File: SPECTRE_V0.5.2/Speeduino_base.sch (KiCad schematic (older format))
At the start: 218 parts, among them J1 Conn_01x06_Male, J2 Conn_02x04_Odd_Even, J3 ProtoArea, Q1 AO3400, Q10 BSP78, Q11 BSP78, Q12 AO3400, Q13 BSP78, Q14 BSP78, Q15 BSP78, Q16 BSP78, Q17 BSP78, Q18 BSP78, Q19 BSP78, Q20 BSP78, Q21 BSP78, Q6 AO3400, Q7 AO3400, Q8 AO3400, Q9 AO3400, U1 MAX9926UAEE+, U2 LM78M05_TO220, U3 TL431DBZ, U4 molex_48pin, U5 TJA1050, U6 MAX3232, U7 MIC4427, U8 MIC4427, U9 MIC4427

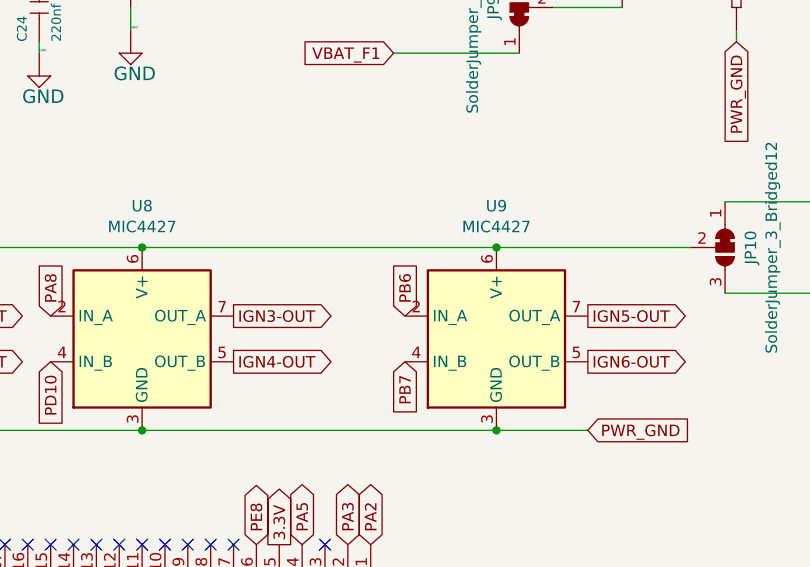
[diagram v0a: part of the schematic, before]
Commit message: Update ign5 pin
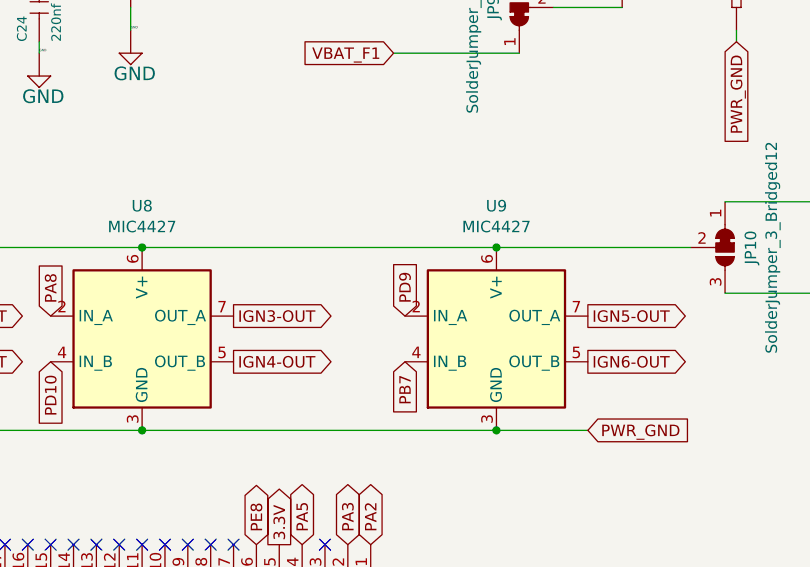
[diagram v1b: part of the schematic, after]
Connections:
- net PB6: no longer U9.2 (IN_A)
- net PD9: now also U9.2 (IN_A)
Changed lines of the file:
@@
 $EndComp
 Text GLabel 8300 9550 1    50   Input ~ 0
-PB6
+PD9
 Text GLabel 9100 10050 2    50   Input ~ 0
 PWR_GND

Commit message: Updates on V0.5.2
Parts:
- removed D24, D25: 1N4007, Diode_SMD:D_SMA, symbol Device:D_Small
- removed JP17: SolderJumper_3_Bridged12, Jumper:SolderJumper-3_P1.3mm_Bridged12_Pad1.0x1.5mm, symbol Jumper:SolderJumper_3_Bridged12
- removed Q8, Q9: AO3400, Speeduino_base:SOT-23, symbol Speeduino_base-eagle-import:SMD-MOSFET-N-CH-20V-2.1A-CJ2302(SOT-23)
- removed R70, R71: 100R, Speeduino_base:R0603, symbol Speeduino_base-eagle-import:SMD-RES-470R-5%-1_10W(0603)
- removed R72, R73: 10k, Speeduino_base:R0603, symbol Speeduino_base-eagle-import:SMD-RES-470R-5%-1_10W(0603)
- added JP18: SolderJumper_3_Bridged12, Jumper:SolderJumper-3_P1.3mm_Bridged12_Pad1.0x1.5mm, symbol Jumper:SolderJumper_3_Bridged12
- added U10: MIC4427, Package_SO:SO-8_3.9x4.9mm_P1.27mm, symbol Driver_FET:MIC4427
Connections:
- net FLEX_FUEL_IN: now also U4.38; no longer JP16.1 (A)
- net GND: now also JP16.1 (A), JP18.1 (A); no longer U4.22, U4.26
- net IGN5-OUT: now also JP18.3 (B); no longer JP16.3 (B)
- net IGN6-OUT: now also JP16.3 (B)
- net PB12: now also U10.2 (IN_A)
- net PB13: now also U10.4 (IN_B)
- net PWR_GND: now also U10.3 (GND)
- net Spare_1-Out: now also U10.5 (OUT_B)
- net Spare_2-Out: now also U10.7 (OUT_A)
- net TACHO-OUT: now also U4.48
- net V_IDLE: now also U10.6 (V+)
- net at JP16.2 (C): now also U4.26; no longer U4.38
- new net: JP18.2 (C), U4.22
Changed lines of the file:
@@
 Text GLabel 6500 1400 3    50   Output ~ 0
 MAP
-Text GLabel 6600 1400 3    50   Input ~ 0
-GND
 Text GLabel 5650 1400 3    50   Output ~ 0
 IAT
@@
 Text GLabel 8850 1400 3    50   Input ~ 0
 3.3V
-Text GLabel 8200 2050 3    50   Output ~ 0
+Text GLabel 7950 1400 3    50   Output ~ 0
 FLEX_FUEL_IN
-Text GLabel 9350 2000 3    50   Input ~ 0
-TACHO-OUT
 $Comp
 L Jumper:SolderJumper_3_Bridged12 JP8
@@
 Wire Wire Line
 	750  10300 750  10400
-Text GLabel 6200 1400 3    50   Input ~ 0
+Text GLabel 7450 2300 3    50   Input ~ 0
 GND
 Text GLabel 7050 1400 3    50   Input ~ 0
@@
 Wire Wire Line
 	4050 11100 4050 11200
-Text GLabel 11850 9400 2    50   Input ~ 0
+Text GLabel 11800 9500 2    50   Input ~ 0
 PWR_GND
-Text GLabel 12300 8850 1    50   Output ~ 0
+Text GLabel 12150 8950 2    50   Output ~ 0
 Spare_2-Out
-Text GLabel 11950 8550 0    50   Input ~ 0
-VBAT
-Wire Wire Line
-	11400 9400 11800 9400
-Wire Wire Line
-	11400 9050 11600 9050
-Wire Wire Line
-	11250 9000 11400 9000
-Wire Wire Line
-	11400 9000 11400 9050
-Connection ~ 11400 9050
-Wire Wire Line
-	11400 9350 11400 9400
-Wire Wire Line
-	11800 9400 11800 9250
-Wire Wire Line
-	11800 8850 11950 8850
-$Comp
-L Speeduino_base-eagle-import:SMD-RES-470R-5%-1_10W(0603) R73
-U 1 1 5F3D9256
-P 11400 9200
-F 0 "R73" H 11250 9250 42  0000 L BNN
-F 1 "10k" H 11250 9100 42  0000 L BNN
-F 2 "Speeduino_base:R0603" H 11400 9200 50  0001 C CNN
-F 3 "" H 11400 9200 50  0001 C CNN
-	1    11400 9200
-	0    1    1    0
-$EndComp
-$Comp
-L Speeduino_base-eagle-import:SMD-RES-470R-5%-1_10W(0603) R71
-U 1 1 5F3D9262
-P 11100 9000
-F 0 "R71" H 10950 9050 42  0000 L BNN
-F 1 "100R" H 10950 8900 42  0000 L BNN
-F 2 "Speeduino_base:R0603" H 11100 9000 50  0001 C CNN
-F 3 "" H 11100 9000 50  0001 C CNN
-	1    11100 9000
-	1    0    0    -1
-$EndComp
-$Comp
-L Speeduino_base-eagle-import:SMD-MOSFET-N-CH-20V-2.1A-CJ2302(SOT-23) Q9
-U 1 1 5F3D9268
-P 11800 9050
-F 0 "Q9" H 11650 9150 42  0000 L BNN
-F 1 "AO3400" H 11800 9150 42  0000 L BNN
-F 2 "Speeduino_base:SOT-23" H 11800 9050 50  0001 C CNN
-F 3 "" H 11800 9050 50  0001 C CNN
-	1    11800 9050
-	1    0    0    -1
-$EndComp
-$Comp
-L Device:D_Small D25
-U 1 1 5F3D926E
-P 11950 8750
-F 0 "D25" V 11904 8818 50  0000 L CNN
-F 1 "1N4007" V 11995 8818 50  0000 L CNN
-F 2 "Diode_SMD:D_SMA" V 11950 8750 50  0001 C CNN
-F 3 "~" V 11950 8750 50  0001 C CNN
-	1    11950 8750
-	0    1    1    0
-$EndComp
-Wire Wire Line
-	11950 8850 12300 8850
-Connection ~ 11950 8850
-Text GLabel 10850 9000 1    50   Input ~ 0
+Text GLabel 11750 8650 0    50   Input ~ 0
+V_IDLE
+Text GLabel 11300 9150 0    50   Input ~ 0
 PB13
-Wire Wire Line
-	10850 9000 10950 9000
-Wire Wire Line
-	11850 9400 11800 9400
-Connection ~ 11800 9400
-Wire Wire Line
-	11950 8550 11950 8650
-Text GLabel 11850 8150 2    50   Input ~ 0
-PWR_GND
-Text GLabel 12300 7600 1    50   Output ~ 0
+Text GLabel 12200 9150 2    50   Output ~ 0
 Spare_1-Out
-Text GLabel 11950 7300 0    50   Input ~ 0
-VBAT
-Wire Wire Line
-	11400 8150 11800 8150
-Wire Wire Line
-	11400 7800 11600 7800
-Wire Wire Line
-	11250 7750 11400 7750
-Wire Wire Line
-	11400 7750 11400 7800
-Connection ~ 11400 7800
-Wire Wire Line
-	11400 8100 11400 8150
-Wire Wire Line
-	11800 8150 11800 8000
-Wire Wire Line
-	11800 7600 11950 7600
-$Comp
-L Speeduino_base-eagle-import:SMD-RES-470R-5%-1_10W(0603) R72
-U 1 1 5F7FAD08
-P 11400 7950
-F 0 "R72" H 11250 8000 42  0000 L BNN
-F 1 "10k" H 11250 7850 42  0000 L BNN
-F 2 "Speeduino_base:R0603" H 11400 7950 50  0001 C CNN
-F 3 "" H 11400 7950 50  0001 C CNN
-	1    11400 7950
-	0    1    1    0
-$EndComp
-$Comp
-L Speeduino_base-eagle-import:SMD-RES-470R-5%-1_10W(0603) R70
-U 1 1 5F7FAD0E
-P 11100 7750
-F 0 "R70" H 10950 7800 42  0000 L BNN
-F 1 "100R" H 10950 7650 42  0000 L BNN
-F 2 "Speeduino_base:R0603" H 11100 7750 50  0001 C CNN
-F 3 "" H 11100 7750 50  0001 C CNN
-	1    11100 7750
-	1    0    0    -1
-$EndComp
-$Comp
-L Speeduino_base-eagle-import:SMD-MOSFET-N-CH-20V-2.1A-CJ2302(SOT-23) Q8
-U 1 1 5F7FAD14
-P 11800 7800
-F 0 "Q8" H 11650 7900 42  0000 L BNN
-F 1 "AO3400" H 11800 7900 42  0000 L BNN
-F 2 "Speeduino_base:SOT-23" H 11800 7800 50  0001 C CNN
-F 3 "" H 11800 7800 50  0001 C CNN
-	1    11800 7800
-	1    0    0    -1
-$EndComp
-$Comp
-L Device:D_Small D24
-U 1 1 5F7FAD1A
-P 11950 7500
-F 0 "D24" V 11904 7568 50  0000 L CNN
-F 1 "1N4007" V 11995 7568 50  0000 L CNN
-F 2 "Diode_SMD:D_SMA" V 11950 7500 50  0001 C CNN
-F 3 "~" V 11950 7500 50  0001 C CNN
-	1    11950 7500
-	0    1    1    0
-$EndComp
-Wire Wire Line
-	11950 7600 12300 7600
-Connection ~ 11950 7600
-Text GLabel 10850 7750 1    50   Input ~ 0
+Text GLabel 11350 8950 0    50   Input ~ 0
 PB12
-Wire Wire Line
-	10850 7750 10950 7750
-Wire Wire Line
-	11850 8150 11800 8150
-Connection ~ 11800 8150
-Wire Wire Line
-	11950 7300 11950 7400
 Text GLabel 16450 10950 2    50   Output ~ 0
 INJ8-OUT
@@
 Connection ~ 7150 10050
 Connection ~ 8700 10050
-$Comp
-L Jumper:SolderJumper_3_Bridged12 JP16
-U 1 1 5F69F1FE
-P 7950 2000
-F 0 "JP16" H 7950 2113 50  0000 C CNN
-F 1 "SolderJumper_3_Bridged12" H 7950 2204 50  0000 C CNN
-F 2 "Jumper:SolderJumper-3_P1.3mm_Bridged12_Pad1.0x1.5mm" H 7950 2000 50  0001 C CNN
-F 3 "~" H 7950 2000 50  0001 C CNN
-	1    7950 2000
-	-1   0    0    1
-$EndComp
-Text GLabel 7750 2100 3    50   Input ~ 0
-IGN5-OUT
-Wire Wire Line
-	7750 2000 7750 2100
-Wire Wire Line
-	8150 2000 8200 2000
-Wire Wire Line
-	8200 2000 8200 2050
-Wire Wire Line
-	7950 1400 7950 1850
-$Comp
-L Jumper:SolderJumper_3_Bridged12 JP17
-U 1 1 5F83750C
-P 9150 2000
-F 0 "JP17" H 9150 2113 50  0000 C CNN
-F 1 "SolderJumper_3_Bridged12" H 9150 2204 50  0000 C CNN
-F 2 "Jumper:SolderJumper-3_P1.3mm_Bridged12_Pad1.0x1.5mm" H 9150 2000 50  0001 C CNN
-F 3 "~" H 9150 2000 50  0001 C CNN
-	1    9150 2000
-	-1   0    0    1
-$EndComp
-Text GLabel 8950 2100 3    50   Input ~ 0
-IGN6-OUT
-Wire Wire Line
-	8950 2000 8950 2100
-Wire Wire Line
-	9150 1850 9150 1400
-Wire Wire Line
-	9150 1400 9050 1400
 Text GLabel 7450 11050 3    50   Input ~ 0
 5V
@@
 Text GLabel 2600 2350 3    50   Input ~ 0
 5V
+$Comp
+L Jumper:SolderJumper_3_Bridged12 JP18
+U 1 1 5F36B798
+P 7200 2250
+F 0 "JP18" H 7200 2363 50  0000 C CNN
+F 1 "SolderJumper_3_Bridged12" H 7200 2454 50  0000 C CNN
+F 2 "Jumper:SolderJumper-3_P1.3mm_Bridged12_Pad1.0x1.5mm" H 7200 2250 50  0001 C CNN
+F 3 "~" H 7200 2250 50  0001 C CNN
+	1    7200 2250
+	-1   0    0    1
+$EndComp
+Text GLabel 7000 2350 3    50   Input ~ 0
+IGN5-OUT
+Wire Wire Line
+	7000 2250 7000 2350
+Wire Wire Line
+	7400 2250 7450 2250
+Wire Wire Line
+	7450 2250 7450 2300
+Wire Wire Line
+	7200 2100 6650 2100
+Wire Wire Line
+	6650 2100 6650 1900
+Wire Wire Line
+	6650 1900 6200 1900
+Wire Wire Line
+	6200 1900 6200 1400
+Text GLabel 9050 1400 3    50   Input ~ 0
+TACHO-OUT
+Text GLabel 8100 2300 3    50   Input ~ 0
+GND
+$Comp
+L Jumper:SolderJumper_3_Bridged12 JP16
+U 1 1 5F462689
+P 7850 2250
+F 0 "JP16" H 7850 2363 50  0000 C CNN
+F 1 "SolderJumper_3_Bridged12" H 7850 2454 50  0000 C CNN
+F 2 "Jumper:SolderJumper-3_P1.3mm_Bridged12_Pad1.0x1.5mm" H 7850 2250 50  0001 C CNN
+F 3 "~" H 7850 2250 50  0001 C CNN
+	1    7850 2250
+	-1   0    0    1
+$EndComp
+Text GLabel 7650 2350 3    50   Input ~ 0
+IGN6-OUT
+Wire Wire Line
+	7650 2250 7650 2350
+Wire Wire Line
+	8050 2250 8100 2250
+Wire Wire Line
+	8100 2250 8100 2300
+Wire Wire Line
+	7850 2100 7850 2000
+Wire Wire Line
+	7850 2000 6700 2000
+Wire Wire Line
+	6700 2000 6700 1700
+Wire Wire Line
+	6700 1700 6600 1700
+Wire Wire Line
+	6600 1700 6600 1400
+$Comp
+L Driver_FET:MIC4427 U10
+U 1 1 5F558FC7
+P 11750 9050
+F 0 "U10" H 11750 9631 50  0000 C CNN
+F 1 "MIC4427" H 11750 9540 50  0000 C CNN
+F 2 "Package_SO:SO-8_3.9x4.9mm_P1.27mm" H 11750 8750 50  0001 C CNN
+F 3 "http://ww1.microchip.com/downloads/en/DeviceDoc/mic4426.pdf" H 11750 8750 50  0001 C CNN
+	1    11750 9050
+	1    0    0    -1
+$EndComp
+Wire Wire Line
+	11750 9450 11750 9500
+Wire Wire Line
+	11750 9500 11800 9500
+Wire Wire Line
+	11350 9150 11300 9150
+Wire Wire Line
+	12150 9150 12200 9150
 $EndSCHEMATC

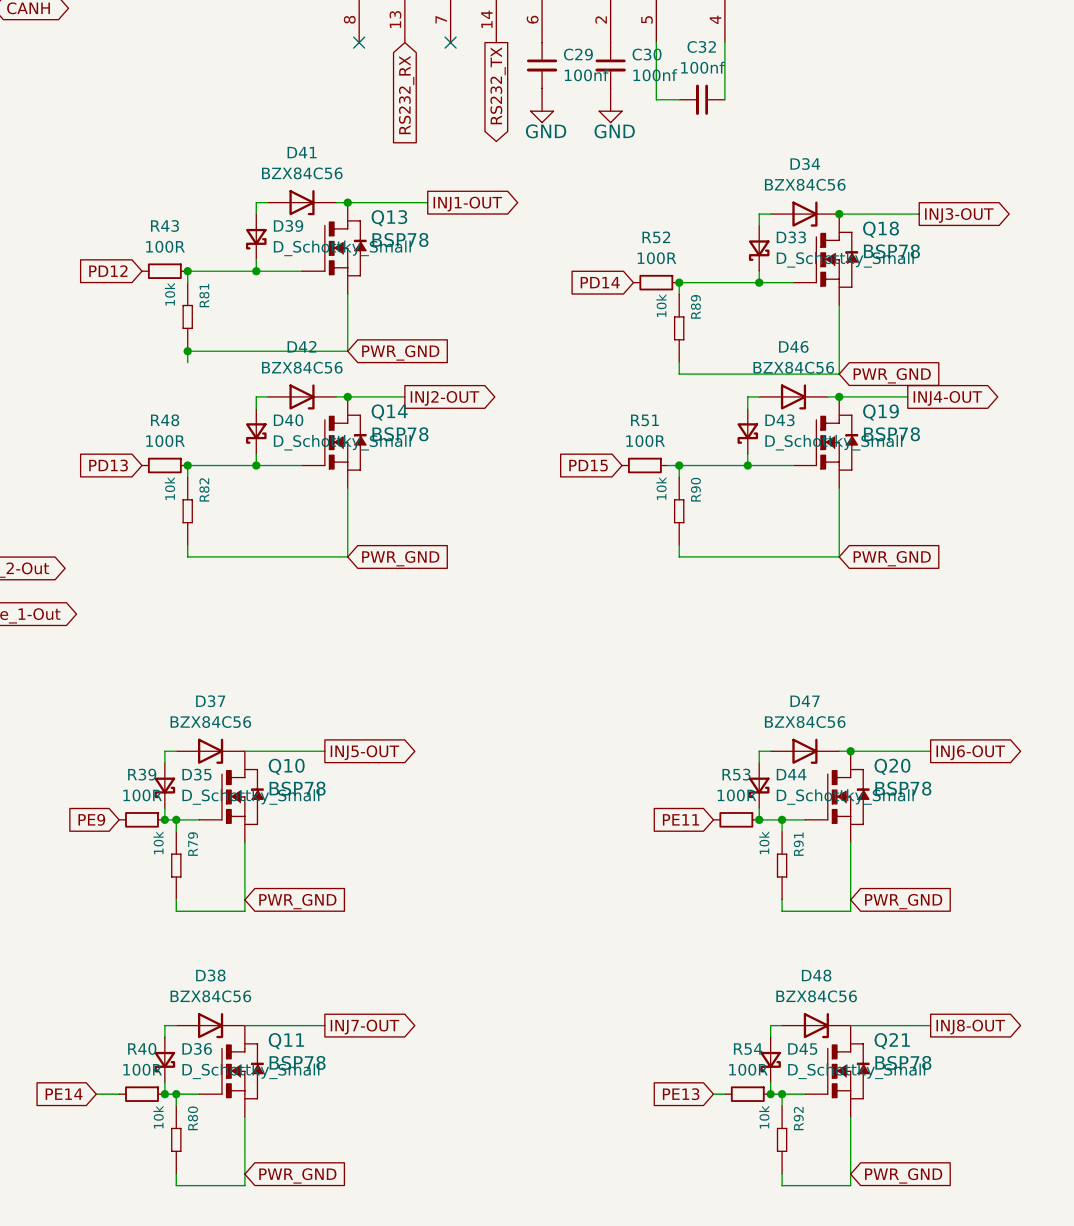
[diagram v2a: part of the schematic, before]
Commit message: Update zener value
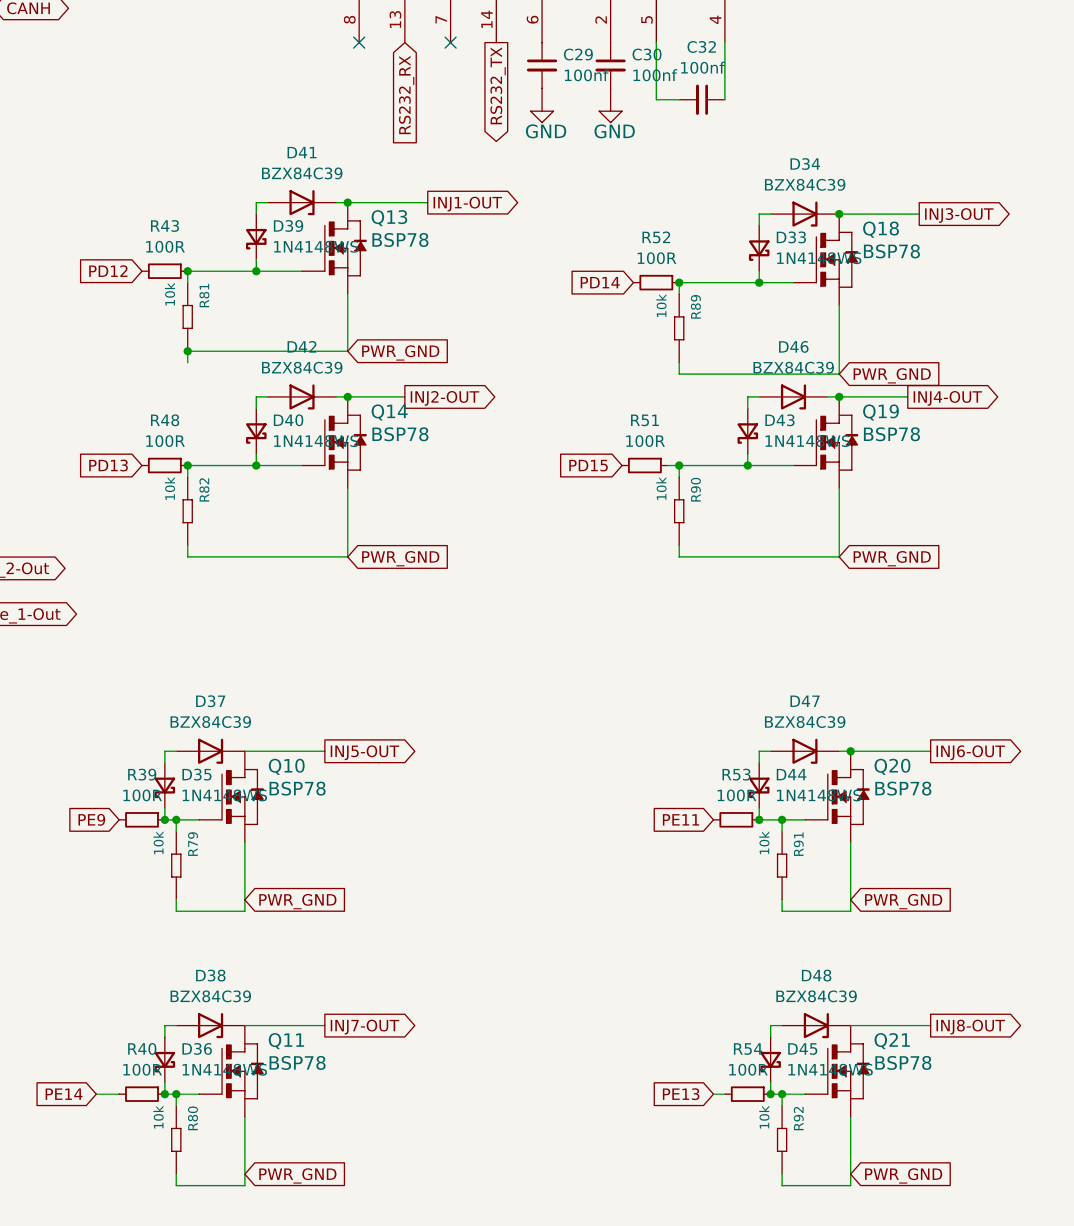
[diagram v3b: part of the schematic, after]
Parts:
- D33, D35, D36, D39, D40, D43, D44, D45: value D_Schottky_Small -> 1N4148WS
- D34, D37, D38, D41, D42, D46, D47, D48: value BZX84C56 -> BZX84C39
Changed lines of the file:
@@
 P 15900 7400
 F 0 "D34" H 15900 7183 50  0000 C CNN
-F 1 "BZX84C56" H 15900 7274 50  0000 C CNN
+F 1 "BZX84C39" H 15900 7274 50  0000 C CNN
 F 2 "Diode_SMD:D_SOT-23_ANK" H 15900 7225 50  0001 C CNN
 F 3 "https://diotec.com/tl_files/diotec/files/pdf/datasheets/bzx84c2v4.pdf" H 15900 7400 50  0001 C CNN
@@
 P 15700 7550
 F 0 "D33" V 15746 7480 50  0000 R CNN
-F 1 "D_Schottky_Small" V 15655 7480 50  0000 R CNN
+F 1 "1N4148WS" V 15655 7480 50  0000 R CNN
 F 2 "Diode_SMD:D_SOD-323" V 15700 7550 50  0001 C CNN
 F 3 "~" V 15700 7550 50  0001 C CNN
@@
 P 15850 8200
 F 0 "D46" H 15850 7983 50  0000 C CNN
-F 1 "BZX84C56" H 15850 8074 50  0000 C CNN
+F 1 "BZX84C39" H 15850 8074 50  0000 C CNN
 F 2 "Diode_SMD:D_SOT-23_ANK" H 15850 8025 50  0001 C CNN
 F 3 "https://diotec.com/tl_files/diotec/files/pdf/datasheets/bzx84c2v4.pdf" H 15850 8200 50  0001 C CNN
@@
 P 15650 8350
 F 0 "D43" V 15696 8280 50  0000 R CNN
-F 1 "D_Schottky_Small" V 15605 8280 50  0000 R CNN
+F 1 "1N4148WS" V 15605 8280 50  0000 R CNN
 F 2 "Diode_SMD:D_SOD-323" V 15650 8350 50  0001 C CNN
 F 3 "~" V 15650 8350 50  0001 C CNN
@@
 P 13700 8200
 F 0 "D42" H 13700 7983 50  0000 C CNN
-F 1 "BZX84C56" H 13700 8074 50  0000 C CNN
+F 1 "BZX84C39" H 13700 8074 50  0000 C CNN
 F 2 "Diode_SMD:D_SOT-23_ANK" H 13700 8025 50  0001 C CNN
 F 3 "https://diotec.com/tl_files/diotec/files/pdf/datasheets/bzx84c2v4.pdf" H 13700 8200 50  0001 C CNN
@@
 P 13500 8350
 F 0 "D40" V 13546 8280 50  0000 R CNN
-F 1 "D_Schottky_Small" V 13455 8280 50  0000 R CNN
+F 1 "1N4148WS" V 13455 8280 50  0000 R CNN
 F 2 "Diode_SMD:D_SOD-323" V 13500 8350 50  0001 C CNN
 F 3 "~" V 13500 8350 50  0001 C CNN
@@
 P 13700 7350
 F 0 "D41" H 13700 7133 50  0000 C CNN
-F 1 "BZX84C56" H 13700 7224 50  0000 C CNN
+F 1 "BZX84C39" H 13700 7224 50  0000 C CNN
 F 2 "Diode_SMD:D_SOT-23_ANK" H 13700 7175 50  0001 C CNN
 F 3 "https://diotec.com/tl_files/diotec/files/pdf/datasheets/bzx84c2v4.pdf" H 13700 7350 50  0001 C CNN
@@
 P 13500 7500
 F 0 "D39" V 13546 7430 50  0000 R CNN
-F 1 "D_Schottky_Small" V 13455 7430 50  0000 R CNN
+F 1 "1N4148WS" V 13455 7430 50  0000 R CNN
 F 2 "Diode_SMD:D_SOD-323" V 13500 7500 50  0001 C CNN
 F 3 "~" V 13500 7500 50  0001 C CNN
@@
 P 13300 9750
 F 0 "D37" H 13300 9533 50  0000 C CNN
-F 1 "BZX84C56" H 13300 9624 50  0000 C CNN
+F 1 "BZX84C39" H 13300 9624 50  0000 C CNN
 F 2 "Diode_SMD:D_SOT-23_ANK" H 13300 9575 50  0001 C CNN
 F 3 "https://diotec.com/tl_files/diotec/files/pdf/datasheets/bzx84c2v4.pdf" H 13300 9750 50  0001 C CNN
@@
 P 13100 9900
 F 0 "D35" V 13146 9830 50  0000 R CNN
-F 1 "D_Schottky_Small" V 13055 9830 50  0000 R CNN
+F 1 "1N4148WS" V 13055 9830 50  0000 R CNN
 F 2 "Diode_SMD:D_SOD-323" V 13100 9900 50  0001 C CNN
 F 3 "~" V 13100 9900 50  0001 C CNN
@@
 P 15900 9750
 F 0 "D47" H 15900 9533 50  0000 C CNN
-F 1 "BZX84C56" H 15900 9624 50  0000 C CNN
+F 1 "BZX84C39" H 15900 9624 50  0000 C CNN
 F 2 "Diode_SMD:D_SOT-23_ANK" H 15900 9575 50  0001 C CNN
 F 3 "https://diotec.com/tl_files/diotec/files/pdf/datasheets/bzx84c2v4.pdf" H 15900 9750 50  0001 C CNN
@@
 P 15700 9900
 F 0 "D44" V 15746 9830 50  0000 R CNN
-F 1 "D_Schottky_Small" V 15655 9830 50  0000 R CNN
+F 1 "1N4148WS" V 15655 9830 50  0000 R CNN
 F 2 "Diode_SMD:D_SOD-323" V 15700 9900 50  0001 C CNN
 F 3 "~" V 15700 9900 50  0001 C CNN
@@
 P 13300 10950
 F 0 "D38" H 13300 10733 50  0000 C CNN
-F 1 "BZX84C56" H 13300 10824 50  0000 C CNN
+F 1 "BZX84C39" H 13300 10824 50  0000 C CNN
 F 2 "Diode_SMD:D_SOT-23_ANK" H 13300 10775 50  0001 C CNN
 F 3 "https://diotec.com/tl_files/diotec/files/pdf/datasheets/bzx84c2v4.pdf" H 13300 10950 50  0001 C CNN
@@
 P 13100 11100
 F 0 "D36" V 13146 11030 50  0000 R CNN
-F 1 "D_Schottky_Small" V 13055 11030 50  0000 R CNN
+F 1 "1N4148WS" V 13055 11030 50  0000 R CNN
 F 2 "Diode_SMD:D_SOD-323" V 13100 11100 50  0001 C CNN
 F 3 "~" V 13100 11100 50  0001 C CNN
@@
 P 15950 10950
 F 0 "D48" H 15950 10733 50  0000 C CNN
-F 1 "BZX84C56" H 15950 10824 50  0000 C CNN
+F 1 "BZX84C39" H 15950 10824 50  0000 C CNN
 F 2 "Diode_SMD:D_SOT-23_ANK" H 15950 10775 50  0001 C CNN
 F 3 "https://diotec.com/tl_files/diotec/files/pdf/datasheets/bzx84c2v4.pdf" H 15950 10950 50  0001 C CNN
@@
 P 15750 11100
 F 0 "D45" V 15796 11030 50  0000 R CNN
-F 1 "D_Schottky_Small" V 15705 11030 50  0000 R CNN
+F 1 "1N4148WS" V 15705 11030 50  0000 R CNN
 F 2 "Diode_SMD:D_SOD-323" V 15750 11100 50  0001 C CNN
 F 3 "~" V 15750 11100 50  0001 C CNN
